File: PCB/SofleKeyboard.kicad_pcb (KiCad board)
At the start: 2 copper layers, 87 parts, among them J1 LED, J2 4PIN, J3 OLED, P1 i2c_pin, P2 i2c_pin, SW1 SW_PUSH, SW10 SW_PUSH, SW11 SW_PUSH, SW12 SW_PUSH, SW13 SW_PUSH, SW14 SW_PUSH, SW15 SW_PUSH, SW16 SW_PUSH, SW17 SW_PUSH, SW18 SW_PUSH, SW19 SW_PUSH, SW2 SW_PUSH, SW20 SW_PUSH, SW21 SW_PUSH, SW22 SW_PUSH, SW23 SW_PUSH, SW24 SW_PUSH, SW25 Rotary_Encoder_Switch, SW26 SW_PUSH, SW27 SW_PUSH, SW28 SW_PUSH, SW29 SW_PUSH, SW3 SW_PUSH, SW30 SW_PUSH, SW4 SW_PUSH, SW5 SW_PUSH, SW6 SW_PUSH, SW7 SW_PUSH, SW8 SW_PUSH, SW9 SW_PUSH, U1 ProMicro

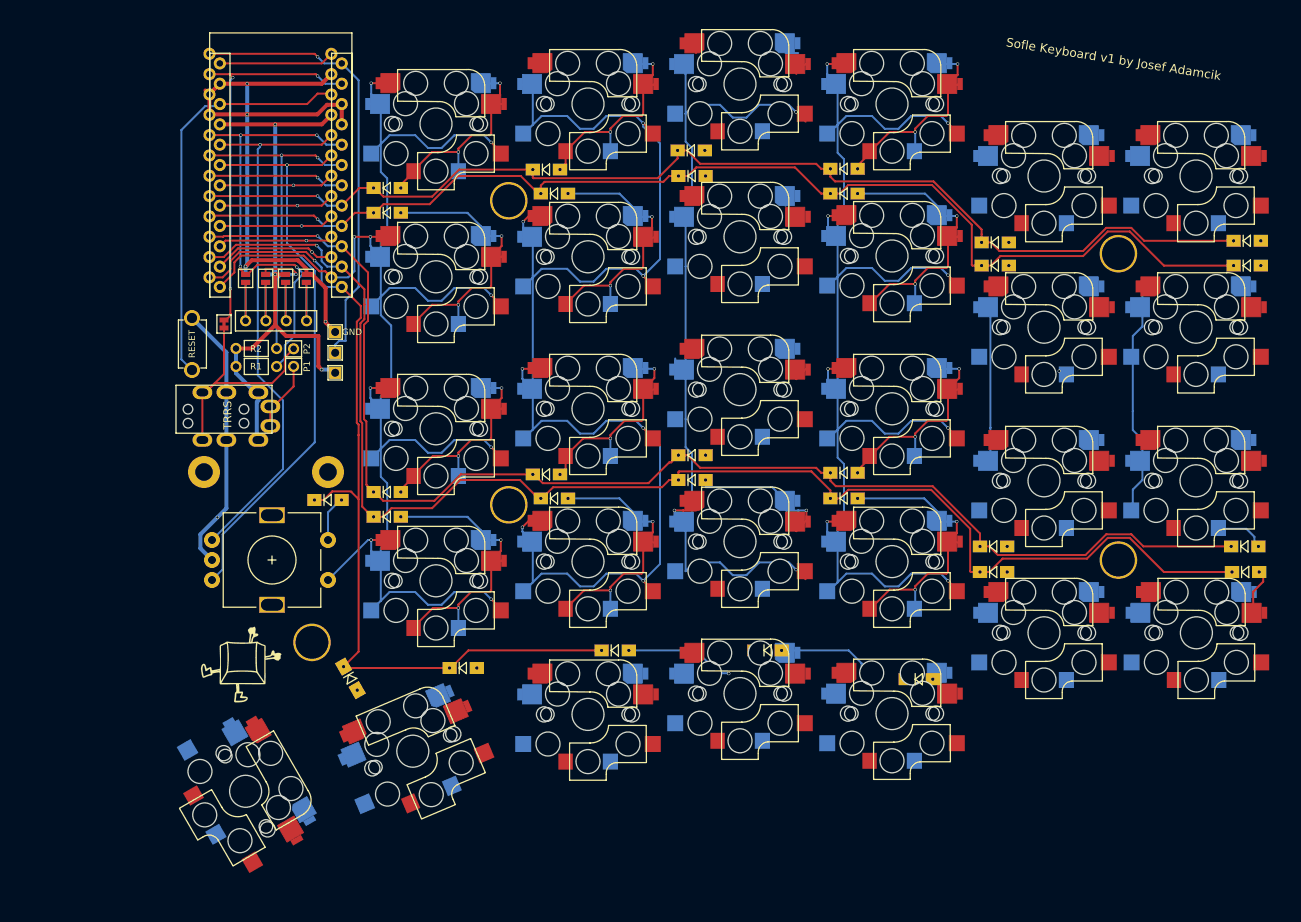
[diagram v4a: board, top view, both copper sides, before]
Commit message: Add footprints for MX only socketed switches. Use those switches on the board
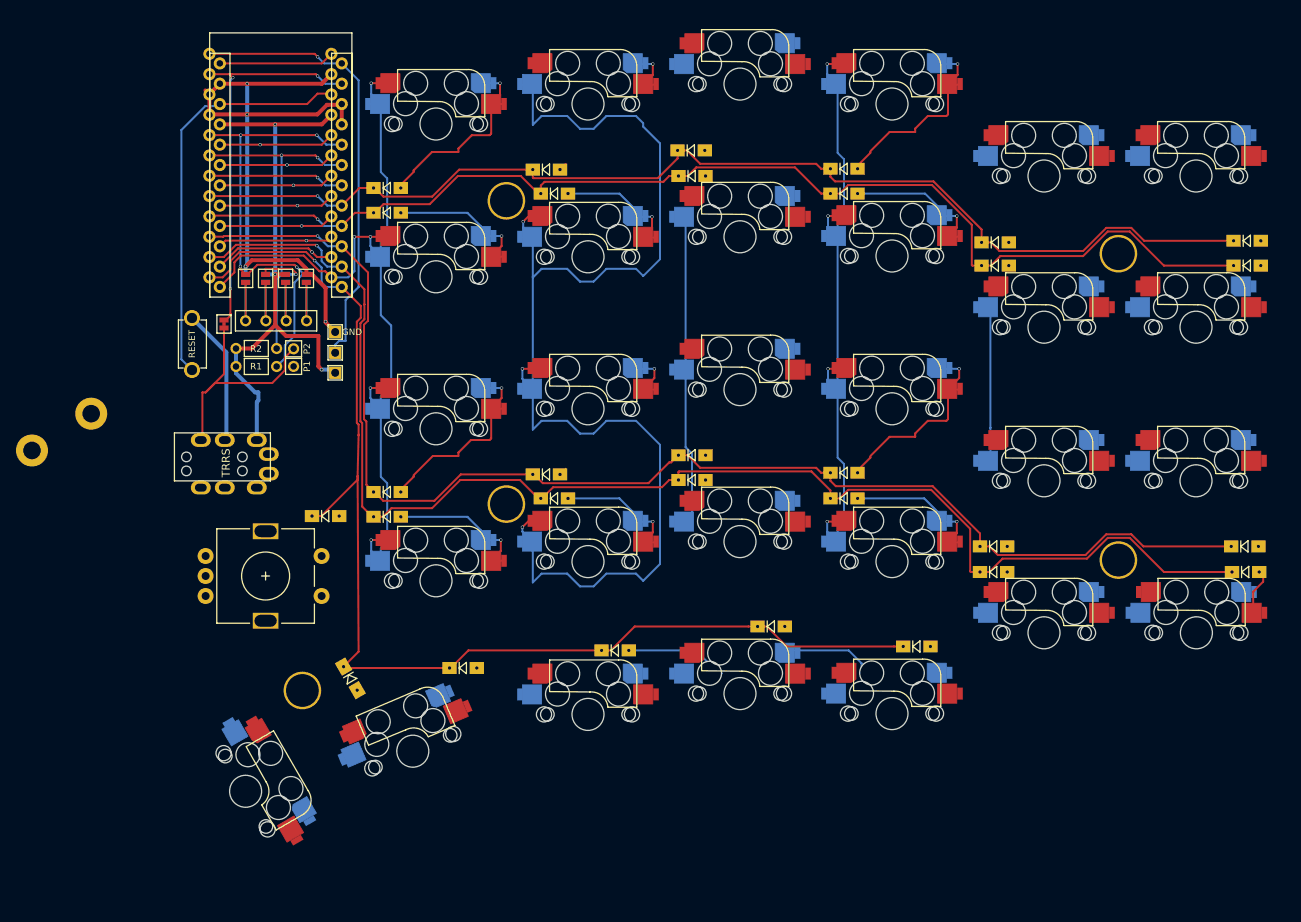
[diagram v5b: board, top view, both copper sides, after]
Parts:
- removed Ref** (x2): Val**, SofleKeyboard-footprint:SofleLogoSmall
- SW1, SW10, SW11, SW12, SW13, SW14, SW15, SW16, SW17, SW18, SW19, SW2, SW20, SW21, SW22, SW23, SW24, SW27, SW28, SW29, SW3, SW30, SW4, SW5, SW6, SW7, SW8, SW9: footprint SofleKeyboard-footprint:CherryMX_KailhLowProfile_Hotswap -> SofleKeyboard-footprint:CherryMX_Hotswap
- SW26: footprint SofleKeyboard-footprint:CherryMX_KailhLowProfile_Hotswap_1.5 -> SofleKeyboard-footprint:CherryMX_Hotswap_1.5
- moved TH2 30.5 mm to (77.4, 86.2)
- moved TH1 21.7 mm to (70.0, 90.8)
- moved TH7 6.13 mm to (103.8, 120.8)
- moved J2 5.96 mm to (87.8, 91.6)
- moved D30 4.10 mm to (180.6, 115.3)
- moved D29 3.02 mm to (162.4, 112.8)
- moved SW25 2.15 mm to (99.2, 106.5)
- moved D25 2.03 mm to (106.7, 99.0)
- moved TH5 0.31 mm to (129.3, 97.5)
- moved TH3 0.30 mm to (129.3, 59.6)
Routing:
- net SW25A: track 206.1 -> 115.4 mm, vias 9 -> 5
- net col2: track 185.2 -> 102.0 mm, vias 9 -> 5
- net col3: track 124.6 -> 50.6 mm, vias 4 -> 1
- net ENCB: track 73.1 -> 14.4 mm
- net ENCA: track 69.0 -> 14.4 mm
- net row4: track 110.7 -> 152.4 mm
- net col0: track 43.6 -> 14.5 mm
- net Net-(D2-Pad2): track 27.9 -> 8.17 mm, vias 2 -> 1
- net Net-(D14-Pad2): track 27.9 -> 8.45 mm, vias 2 -> 1
- net Net-(D19-Pad2): track 37.2 -> 19.1 mm, vias 2 -> 1
- net Net-(D22-Pad2): track 37.1 -> 19.0 mm, vias 2 -> 1
- net Net-(D10-Pad2): track 37.0 -> 18.9 mm, vias 2 -> 1
- net Net-(D8-Pad2): track 35.0 -> 17.0 mm, vias 2 -> 1
- net Net-(D20-Pad2): track 35.2 -> 17.2 mm, vias 2 -> 1
- net Net-(D7-Pad2): track 37.3 -> 19.3 mm, vias 2 -> 1
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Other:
- board text removed: "Sofle Keyboard v1 by Josef Adamcik"

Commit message: WIP routing micro
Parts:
- removed P1, P2: i2c_pin, SofleKeyboard-footprint:1pin_conn
- removed W1: jumper, SofleKeyboard-footprint:jumper_data
- added JP10: IC2SDA, Jumper:SolderJumper-2_P1.3mm_Open_TrianglePad1.0x1.5mm, F.Cu at (101.1, 64.7)
- added JP11: Serial, Jumper:SolderJumper-2_P1.3mm_Bridged2Bar_Pad1.0x1.5mm, B.Cu at (99.8, 64.0)
- added JP9: I2CSCL, Jumper:SolderJumper-2_P1.3mm_Open_TrianglePad1.0x1.5mm, F.Cu at (101.1, 67.4)
- R1, R2: footprint SofleKeyboard-footprint:RESISTOR_mini -> SofleKeyboard-footprint:R_1206_DoubleSided; moved to B.Cu
- U1: footprint SofleKeyboard-footprint:ProMicro -> Keebio:ArduinoProMicro-ZigZag
- moved TH2 31.3 mm to (107.9, 93.4)
- moved R1 24.1 mm to (102.6, 56.6), turned to 270 degrees
- moved RSW1 23.7 mm to (89.3, 53.8), turned to 90 degrees
- moved R2 21.5 mm to (99.4, 56.6), turned to 270 degrees
- moved TH1 20.4 mm to (90.1, 94.0)
- moved J2 7.00 mm to (87.7, 84.6)
- moved U1 5.34 mm to (100.4, 61.3), turned to 270 degrees
- moved JP1 5.00 mm to (104.3, 74.3)
- moved JP2 5.00 mm to (101.7, 74.3)
- moved JP3 5.00 mm to (99.2, 74.3)
- moved JP4 5.00 mm to (96.7, 74.3)
- moved JP5 5.00 mm to (104.3, 74.3)
- moved JP6 5.00 mm to (101.7, 74.3)
- moved JP7 5.00 mm to (99.2, 74.3)
- moved JP8 5.00 mm to (96.7, 74.3)
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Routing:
- net LED: track 55.8 -> 0.00 mm, vias 1 -> 0
- net SW25A: track 115.4 -> 68.4 mm, vias 5 -> 4
- net DATA: track 48.8 -> 16.9 mm, vias 3 -> 1
- net RESET: track 51.2 -> 19.7 mm
- net /i2c_c: track 0.57 -> 24.7 mm, vias 0 -> 1
- net GND: track 99.5 -> 78.1 mm, vias 4 -> 2
- net SDA: track 57.0 -> 36.0 mm, vias 4 -> 2
- net Net-(U1-Pad7): track 17.0 -> 0.00 mm, vias 1 -> 0
- net SCL: track 50.1 -> 33.5 mm, vias 3 -> 2
- net col4: track 181.0 -> 165.7 mm, vias 4 -> 3
- net col0: track 14.5 -> 0.00 mm, vias 1 -> 0
- net col1: track 33.7 -> 19.3 mm, vias 1 -> 0
- net col2: track 102.0 -> 87.5 mm, vias 5 -> 4
- net col3: track 50.6 -> 36.1 mm, vias 1 -> 0
- net Net-(U1-Pad24): track 14.4 -> 0.00 mm
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
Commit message: WIP routing micro
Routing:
- net GND: track 78.1 -> 85.5 mm
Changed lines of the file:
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@@
     (thickness 1.6)
     (drawings 5)
-    (tracks 665)
+    (tracks 669)
     (zones 0)
     (modules 85)
@@
   (segment (start 94 82.51) (end 94 88.46) (width 0.5) (layer F.Cu) (net 34))
   (segment (start 106.338 80.4) (end 107.6 80.4) (width 0.5) (layer F.Cu) (net 34))
-  (segment (start 97.86 80.4) (end 106.338 80.4) (width 0.5) (layer F.Cu) (net 34))
   (segment (start 95.75 82.51) (end 97.86 80.4) (width 0.5) (layer F.Cu) (net 34))
   (segment (start 94 82.51) (end 95.75 82.51) (width 0.5) (layer F.Cu) (net 34))
   (segment (start 94 104.2) (end 91.7 106.5) (width 0.5) (layer F.Cu) (net 34))
   (segment (start 94 88.46) (end 94 104.2) (width 0.5) (layer F.Cu) (net 34))
+  (segment (start 105.5 74.301378) (end 105.5 80.31) (width 0.5) (layer F.Cu) (net 34))
+  (segment (start 104.998242 73.79962) (end 105.5 74.301378) (width 0.5) (layer F.Cu) (net 34))
+  (segment (start 97.86 80.4) (end 105.5 80.31) (width 0.5) (layer F.Cu) (net 34))
+  (segment (start 104.3 73.79962) (end 104.998242 73.79962) (width 0.5) (layer F.Cu) (net 34))
+  (segment (start 105.5 80.31) (end 106.338 80.4) (width 0.5) (layer F.Cu) (net 34))
   (segment (start 189.8 87.96) (end 189.8 93) (width 0.25) (layer B.Cu) (net 36) (status 20))
   (segment (start 189.8 73.8) (end 189.8 87.96) (width 0.25) (layer B.Cu) (net 36) (status 10))

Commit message: WIP routing matrix
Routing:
- net col4: track 165.7 -> 69.2 mm, vias 3 -> 4
- net col0: track 0.00 -> 67.5 mm, vias 0 -> 4
- net col1: track 19.3 -> 65.9 mm, vias 0 -> 4
- net col3: track 36.1 -> 65.8 mm, vias 0 -> 4
- net Net-(D17-Pad2): track 0.28 -> 22.1 mm, vias 0 -> 1
- net Net-(D5-Pad2): track 0.00 -> 21.7 mm, vias 0 -> 1
- net Net-(D3-Pad2): track 0.00 -> 21.7 mm, vias 0 -> 1
- net Net-(D15-Pad2): track 0.00 -> 21.5 mm, vias 0 -> 1
- net Net-(D21-Pad2): track 0.00 -> 17.0 mm, vias 0 -> 1
- net Net-(D23-Pad2): track 0.15 -> 17.1 mm, vias 0 -> 1
- net Net-(D11-Pad2): track 0.28 -> 17.2 mm, vias 0 -> 1
- net Net-(D14-Pad2): track 8.45 -> 25.4 mm
- net Net-(D2-Pad2): track 8.17 -> 25.1 mm
- net Net-(D9-Pad2): track 0.00 -> 16.8 mm, vias 0 -> 1
- net Net-(D18-Pad2): track 0.00 -> 14.9 mm, vias 0 -> 1
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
